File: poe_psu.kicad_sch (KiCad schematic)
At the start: 41 parts, among them T1 HR051142, U2 SI3404-A-GM, U3 EL3H7-G, U4 AN431

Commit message: Switch to LCSC RJ45 socket
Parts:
- L3: LCSC (none) -> C356979
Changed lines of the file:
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@@
+      (effects (font (size 1.27 1.27)) hide)
+    )
+    (property "LCSC" "C356979" (id 4) (at 43.815 104.14 90)
       (effects (font (size 1.27 1.27)) hide)
     )

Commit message: Kicad updates, added missing resistances
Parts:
- C15, R15: now not fitted
- C18: value C -> 100n 100V; LCSC (none) -> C696916
- C21: value C -> 1n 100V; LCSC (none) -> C282513
- L3: LCSC C356979 -> (none)
- R16: value R -> 130K
- R18: value R -> 0
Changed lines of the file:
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@@
 			)
 		)
-		(property "Datasheet" "https://datasheet.lcsc.com/lcsc/2009171138_TAI-TECH-HCB1608KF-501T20_C356979.pdf"
+		(property "Datasheet" ""
 			(at 43.815 81.28 0)
 			(effects
@@
 			)
 		)
-		(property "Datasheet" "https://datasheet.lcsc.com/lcsc/2004140934_Slkor-SLKORMICRO-Elec--SS54_C513478.pdf"
+		(property "Datasheet" ""
 			(at 224.155 63.5 0)
 			(effects
@@
 			)
 		)
-		(property "Datasheet" "https://datasheet.lcsc.com/lcsc/2110091730_Sunlord-UPZ2012E601-2R0TF_C98308.pdf"
+		(property "Datasheet" ""
 			(at 262.89 63.5 0)
 			(effects
@@
 			)
 		)
-		(property "Datasheet" "https://datasheet.lcsc.com/lcsc/1912111437_Slkor-SLKORMICRO-Elec--1N4148W_C444720.pdf"
+		(property "Datasheet" ""
 			(at 166.37 63.5 0)
 			(effects
@@
 			)
 		)
-		(property "Datasheet" "https://datasheet.lcsc.com/lcsc/1811091923_Everlight-Elec-EL3H7-C-TA-G_C92243.pdf"
+		(property "Datasheet" ""
 			(at 187.96 127.635 0)
 			(effects
@@
 			)
 		)
-		(property "Datasheet" "https://datasheet.lcsc.com/lcsc/2108241830_SILICON-LABS-SI3404-A-GMR_C461934.pdf"
+		(property "Datasheet" ""
 			(at 110.49 95.885 0)
 			(effects
@@
 			)
 		)
-		(property "Value" "R"
+		(property "Value" "0"
 			(at 228.6 126.365 90)
 			(effects
@@
 			)
 		)
-		(property "Datasheet" "https://datasheet.lcsc.com/lcsc/1811082114_YAGEO-RC0603FR-0743KL_C137719.pdf"
+		(property "Datasheet" ""
 			(at 257.175 121.92 0)
 			(effects
@@
 			)
 		)
-		(property "LCSC" "C356979"
-			(at 43.815 104.14 90)
-			(effects
-				(font
-					(size 1.27 1.27)
-				)
-				(hide yes)
-			)
-		)
 		(pin "1"
 		)
@@
 		(in_bom yes)
 		(on_board yes)
-		(dnp no)
+		(dnp yes)
 		(fields_autoplaced yes)
 		(property "Reference" "C15"
@@
 			)
 		)
-		(property "Datasheet" "https://datasheet.lcsc.com/lcsc/1809291522_Guangdong-Hottech-1N4148WS_C181133.pdf"
+		(property "Datasheet" ""
 			(at 180.34 73.66 0)
 			(effects
@@
 		(dnp no)
 		(property "Reference" "C18"
-			(at 167.64 50.8 0)
+			(at 168.91 46.228 0)
 			(effects
 				(font
@@
 			)
 		)
-		(property "Value" "C"
-			(at 168.91 53.34 0)
+		(property "Value" "100n 100V"
+			(at 168.91 48.768 0)
 			(effects
 				(font
@@
 			)
 		)
+		(property "LCSC" "C696916"
+			(at 174.625 52.705 0)
+			(effects
+				(font
+					(size 1.27 1.27)
+				)
+				(hide yes)
+			)
+		)
 		(pin "1"
 		)
@@
 			)
 		)
-		(property "Datasheet" "https://datasheet.lcsc.com/lcsc/2209291730_TWGMC-SMDJ58A_C4154735.pdf"
+		(property "Datasheet" ""
 			(at 63.5 92.075 0)
 			(effects
@@
 			)
 		)
-		(property "Datasheet" "https://datasheet.lcsc.com/lcsc/1811082124_YAGEO-RC0603FR-0711K3L_C137803.pdf"
+		(property "Datasheet" ""
 			(at 257.175 137.795 0)
 			(effects
@@
 			)
 		)
-		(property "Value" "R"
+		(property "Value" "130K"
 			(at 160.02 54.6099 0)
 			(effects
@@
 			)
 		)
-		(property "Datasheet" "https://datasheet.lcsc.com/lcsc/2110091730_Sunlord-UPZ2012E601-2R0TF_C98308.pdf"
+		(property "Datasheet" ""
 			(at 262.89 78.74 0)
 			(effects
@@
 			)
 		)
-		(property "Datasheet" "https://www.diodes.com/assets/Datasheets/AN431.pdf"
+		(property "Datasheet" ""
 			(at 208.915 142.24 0)
 			(effects
@@
 			)
 		)
-		(property "Value" "C"
+		(property "Value" "1n 100V"
 			(at 216.535 125.095 90)
 			(effects
@@
 			)
 		)
+		(property "LCSC" "C282513"
+			(at 216.535 130.175 90)
+			(effects
+				(font
+					(size 1.27 1.27)
+				)
+				(hide yes)
+			)
+		)
 		(pin "1"
 		)
@@
 		(in_bom yes)
 		(on_board yes)
-		(dnp no)
+		(dnp yes)
 		(fields_autoplaced yes)
 		(property "Reference" "R15"
@@
 			)
 		)
-		(property "Datasheet" "https://datasheet.lcsc.com/lcsc/1809211119_HANRUN-Zhongshan-HanRun-Elec-HR051142_C55680.pdf"
+		(property "Datasheet" ""
 			(at 201.93 83.82 0)
 			(effects
@@
 			)
 		)
-		(property "Datasheet" "https://datasheet.lcsc.com/lcsc/1912111437_PSA-Prosperity-Dielectrics-FV31X102K202PXG_C363565.pdf"
+		(property "Datasheet" ""
 			(at 201.295 86.995 0)
 			(effects

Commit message: Update schematic for V1.1
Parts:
- R11: value 24.3 1% -> 24.3k 1%; LCSC C3016118 -> C276290
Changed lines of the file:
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@@
 			)
 		)
-		(property "Datasheet" ""
+		(property "Datasheet" "https://www.skyworksinc.com/-/media/Skyworks/SL/documents/public/data-sheets/si3404-datasheet.pdf"
 			(at 110.49 95.885 0)
 			(effects
@@
 			)
 		)
-		(property "Value" "24.3 1%"
+		(property "Value" "24.3k 1%"
 			(at 81.28 92.075 90)
 			(effects
@@
 			)
 		)
-		(property "LCSC" "C3016118"
+		(property "LCSC" "C276290"
 			(at 81.28 88.265 90)
 			(effects

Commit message: BOM updates & schematic fixes
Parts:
- added TP17: POE+, TestPoint:TestPoint_Pad_D1.5mm, symbol Connector:TestPoint
- added TP18: POE-, TestPoint:TestPoint_Pad_D1.5mm, symbol Connector:TestPoint
- added TP19: VT15, TestPoint:TestPoint_Pad_D1.5mm, symbol Connector:TestPoint
- added TP20: EROUT, TestPoint:TestPoint_Pad_D1.5mm, symbol Connector:TestPoint
- added TP21: FBH, TestPoint:TestPoint_Pad_D1.5mm, symbol Connector:TestPoint
- added TP22: OPTO_IN, TestPoint:TestPoint_Pad_D1.5mm, symbol Connector:TestPoint
- added TP23: VSS, TestPoint:TestPoint_Pad_D1.5mm, symbol Connector:TestPoint
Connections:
- net VSS: now also TP23.1
- net VT15: now also TP19.1
- net at C12.1, C13.1, C14.1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: now also TP17.1, TP21.1
- net at C12.2, D2.2 (A), L3.2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: now also TP18.1
- net at R13.2, R15.1, U2.3 (EROUT)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: now also TP20.1
- net at R18.2, R20.2, R21.1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: now also TP22.1

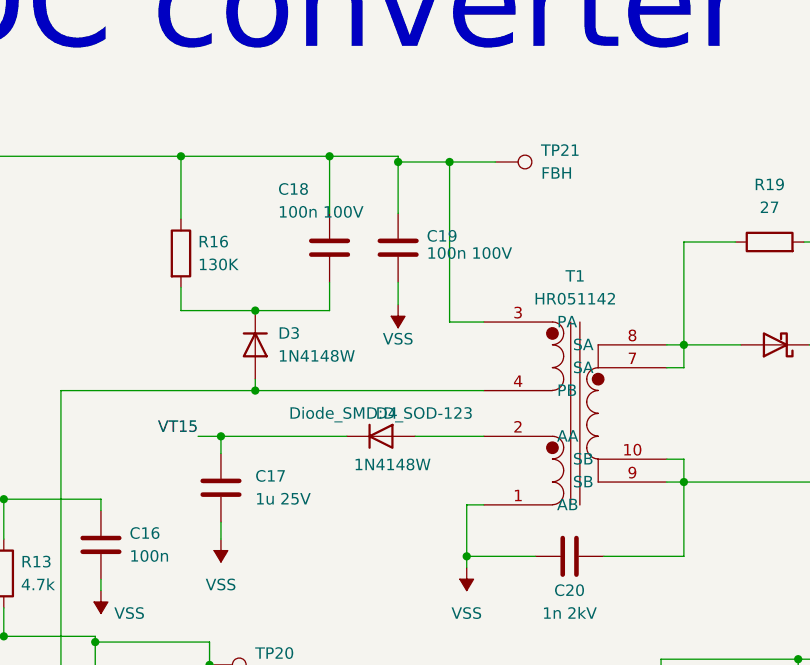
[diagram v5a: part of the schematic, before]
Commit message: fix PoE transofrmer polarity, add more relay outputs
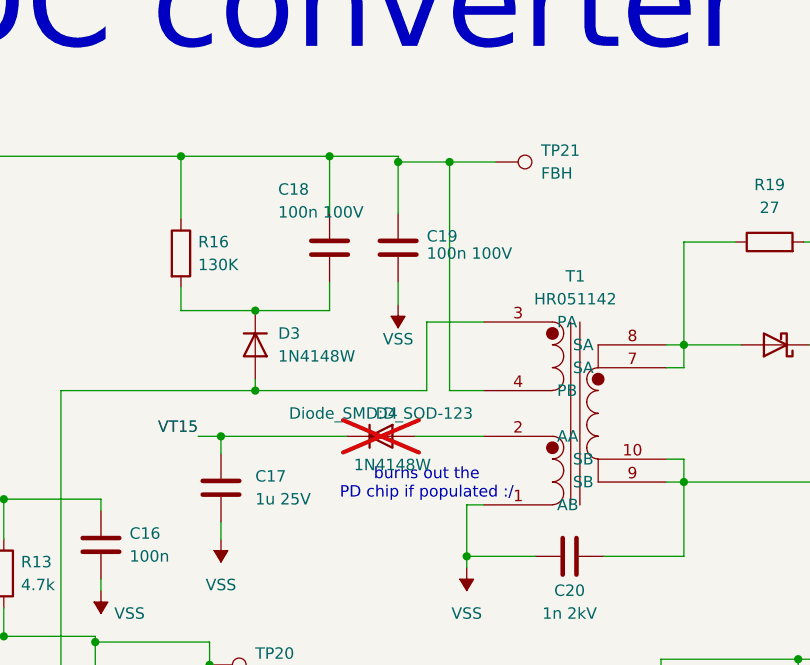
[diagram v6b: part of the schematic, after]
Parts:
- D4: now not fitted
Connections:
- net at C12.1, C13.1, C14.1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: now also T1.4 (PB); no longer T1.3 (PA)
- net at D3.2 (A), U2.18 (SWO): now also T1.3 (PA); no longer T1.4 (PB)
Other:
- note added: "burns out the PD chip if populated :/"
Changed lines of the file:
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@@
 		)
 	)
+	(text "burns out the \nPD chip if populated :/"
+		(exclude_from_sim no)
+		(at 185.42 78.994 0)
+		(effects
+			(font
+				(size 1.27 1.27)
+			)
+		)
+	)
 	(junction
 		(at 92.71 60.96)
@@
 	)
 	(junction
-		(at 166.37 68.58)
-		(diameter 0)
-		(color 0 0 0 0)
-	)
-	(junction
 		(at 138.43 80.645)
 		(diameter 0)
@@
 	)
 	(junction
+		(at 166.37 68.58)
+		(diameter 0)
+		(color 0 0 0 0)
+	)
+	(junction
 		(at 257.175 130.175)
 		(diameter 0)
@@
 	(wire
 		(pts
-			(xy 187.96 43.18) (xy 187.96 60.96)
+			(xy 187.96 43.18) (xy 187.96 68.58)
 		)
 		(stroke
@@
 	(wire
 		(pts
+			(xy 187.96 68.58) (xy 191.77 68.58)
+		)
+		(stroke
+			(width 0)
+			(type default)
+		)
+	)
+	(wire
+		(pts
 			(xy 162.56 73.66) (xy 176.53 73.66)
 		)
@@
 	(wire
 		(pts
+			(xy 185.42 60.96) (xy 191.77 60.96)
+		)
+		(stroke
+			(width 0)
+			(type default)
+		)
+	)
+	(wire
+		(pts
 			(xy 257.175 130.175) (xy 257.175 130.81)
 		)
@@
 	(wire
 		(pts
+			(xy 166.37 68.58) (xy 185.42 68.58)
+		)
+		(stroke
+			(width 0)
+			(type default)
+		)
+	)
+	(wire
+		(pts
 			(xy 257.175 130.81) (xy 257.175 133.985)
 		)
@@
 	(wire
 		(pts
-			(xy 149.225 89.535) (xy 149.225 90.805)
+			(xy 185.42 68.58) (xy 185.42 60.96)
 		)
 		(stroke
@@
 	(wire
 		(pts
-			(xy 276.225 78.74) (xy 278.13 78.74)
+			(xy 149.225 89.535) (xy 149.225 90.805)
 		)
 		(stroke
@@
 	(wire
 		(pts
-			(xy 31.75 81.28) (xy 31.75 88.265)
+			(xy 276.225 78.74) (xy 278.13 78.74)
 		)
 		(stroke
@@
 	(wire
 		(pts
-			(xy 160.02 73.66) (xy 162.56 73.66)
+			(xy 31.75 81.28) (xy 31.75 88.265)
 		)
 		(stroke
@@
 	(wire
 		(pts
-			(xy 86.995 103.505) (xy 90.17 103.505)
+			(xy 160.02 73.66) (xy 162.56 73.66)
 		)
 		(stroke
@@
 	(wire
 		(pts
-			(xy 189.865 88.265) (xy 189.865 86.995)
+			(xy 86.995 103.505) (xy 90.17 103.505)
 		)
 		(stroke
@@
 	(wire
 		(pts
-			(xy 158.115 59.69) (xy 158.115 57.15)
+			(xy 189.865 88.265) (xy 189.865 86.995)
 		)
 		(stroke
@@
 	(wire
 		(pts
-			(xy 187.96 60.96) (xy 191.77 60.96)
+			(xy 158.115 59.69) (xy 158.115 57.15)
 		)
 		(stroke
@@
 	(wire
 		(pts
-			(xy 166.37 68.58) (xy 191.77 68.58)
-		)
-		(stroke
-			(width 0)
-			(type default)
-		)
-	)
-	(wire
-		(pts
 			(xy 92.71 60.96) (xy 133.35 60.96)
 		)
@@
 		(in_bom yes)
 		(on_board yes)
-		(dnp no)
+		(dnp yes)
 		(property "Reference" "D4"
 			(at 180.975 71.12 0)

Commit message: DO the bulk of rev 1.2 layout
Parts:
- D6: value 12V -> PESD15VL1BA; footprint Diode_SMD:D_SMA-SMB_Universal_Handsoldering -> Diode_SMD:D_SOD-323; LCSC (none) -> C18723438
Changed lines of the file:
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@@
 			)
 		)
-		(property "Datasheet" ""
+		(property "Datasheet" "https://www.tme.eu/Document/fa31fd9d447141494f76dc7ecda43c76/EL3H7-G.pdf"
 			(at 187.96 127.635 0)
 			(effects
@@
 			)
 		)
-		(property "Value" "12V"
+		(property "Value" "PESD15VL1BA"
 			(at 275.59 72.3899 90)
 			(effects
@@
 			)
 		)
-		(property "Footprint" "Diode_SMD:D_SMA-SMB_Universal_Handsoldering"
+		(property "Footprint" "Diode_SMD:D_SOD-323"
 			(at 273.05 71.12 0)
 			(effects
@@
 			(effects
 				(font
+					(size 1.27 1.27)
+				)
+				(hide yes)
+			)
+		)
+		(property "LCSC" "C18723438"
+			(at 273.05 71.12 90)
+			(effects
+				(font

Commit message: Use kicad symbol for the optotransistor
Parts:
- T1: footprint project specific:HR051142 -> project_footprints:HR051142
- U2: footprint project specific:QFN50P400X400X90-21N -> project_footprints:QFN50P400X400X90-21N
- U3: footprint project specific:SOIC127P700X200-4N -> project_footprints:SOIC127P700X200-4N
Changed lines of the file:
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@@
 			)
 		)
-		(property "Footprint" "project specific:SOIC127P700X200-4N"
+		(property "Footprint" "project_footprints:SOIC127P700X200-4N"
 			(at 187.96 127.635 0)
 			(effects
@@
 			)
 		)
-		(property "Footprint" "project specific:QFN50P400X400X90-21N"
+		(property "Footprint" "project_footprints:QFN50P400X400X90-21N"
 			(at 110.49 95.885 0)
 			(effects
@@
 			)
 		)
-		(property "Footprint" "project specific:HR051142"
+		(property "Footprint" "project_footprints:HR051142"
 			(at 201.93 83.82 0)
 			(effects
